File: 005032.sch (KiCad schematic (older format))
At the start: 38 parts, among them J1 alim+conn, J2 PROG_ESP02, J4 JTAG, SW1 DMR02, SW2 434153017835, SW3 434153017835, U1 ESP32-WROOM-32E, U2 AP63201, U3 AP63357

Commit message: v5 - commit prima di esecuzione modifiche v6
Signed-off-by: Andrea Toninelli <tonazza@yahoo.it>
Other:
- note added: "MODULO MCU - WIFI"
- note removed: "MODULO MCU"
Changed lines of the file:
@@
 NoConn ~ 3200 3200
 Text Notes 850  850  0    118  ~ 0
-MODULO MCU
+MODULO MCU - WIFI
 Wire Notes Line
 	7000 1750 7000 550

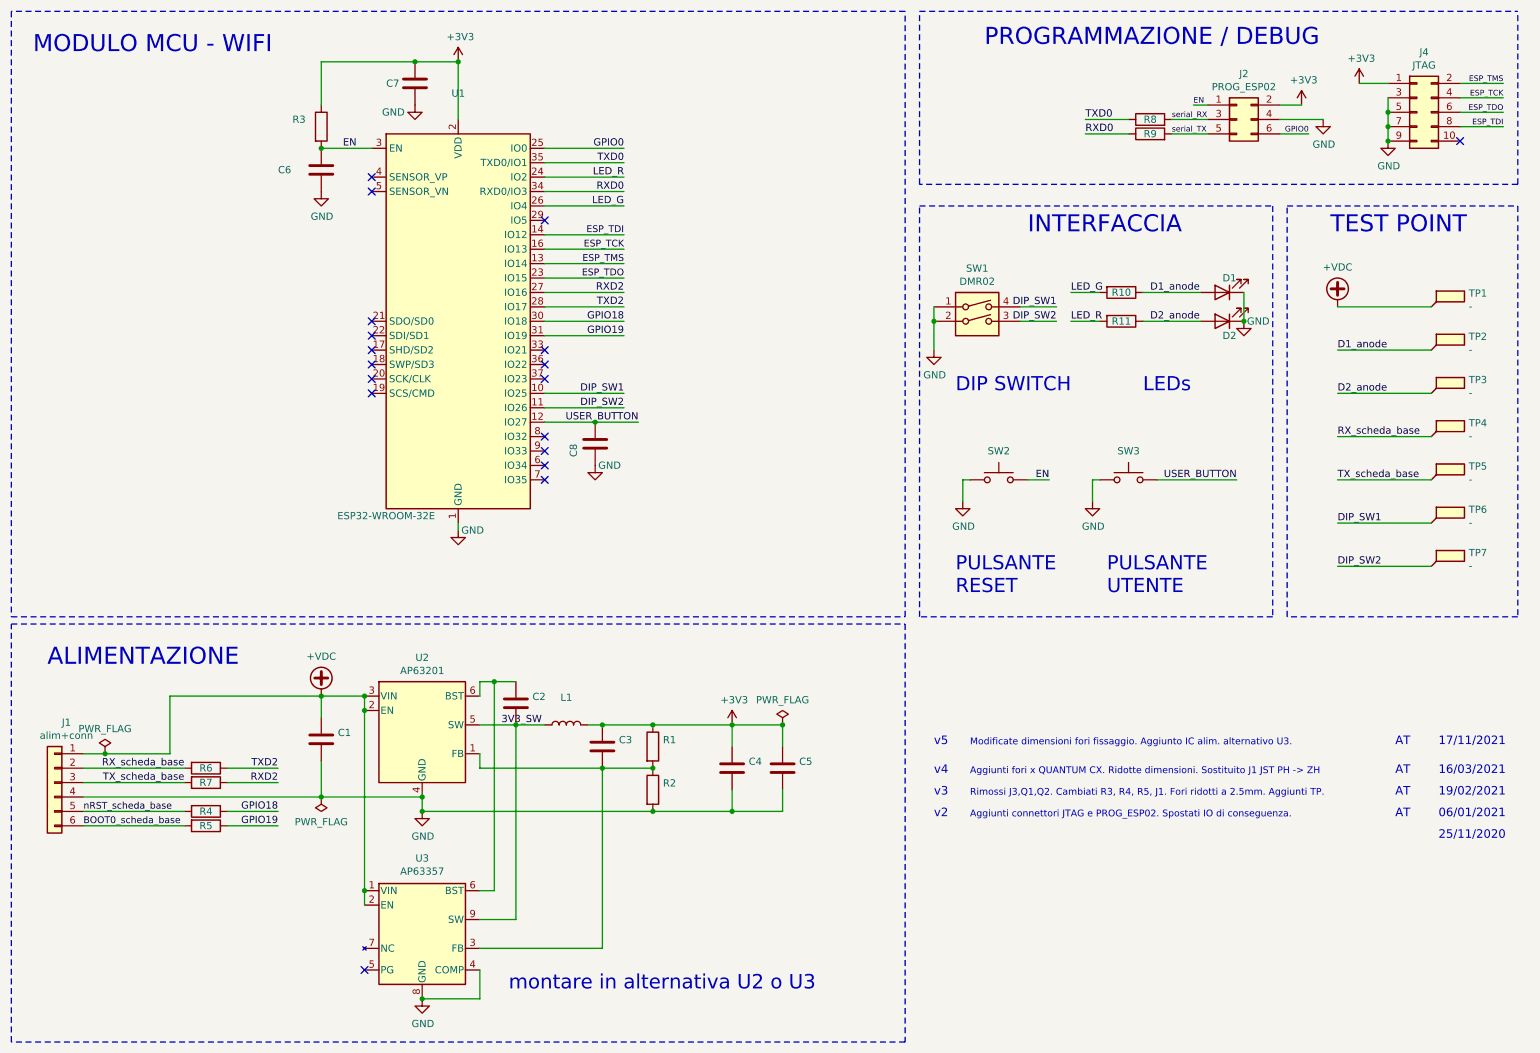
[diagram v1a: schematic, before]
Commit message: v6 - modificato schema (PCB ancora in v5)
Signed-off-by: Andrea Toninelli <tonazza@yahoo.it>
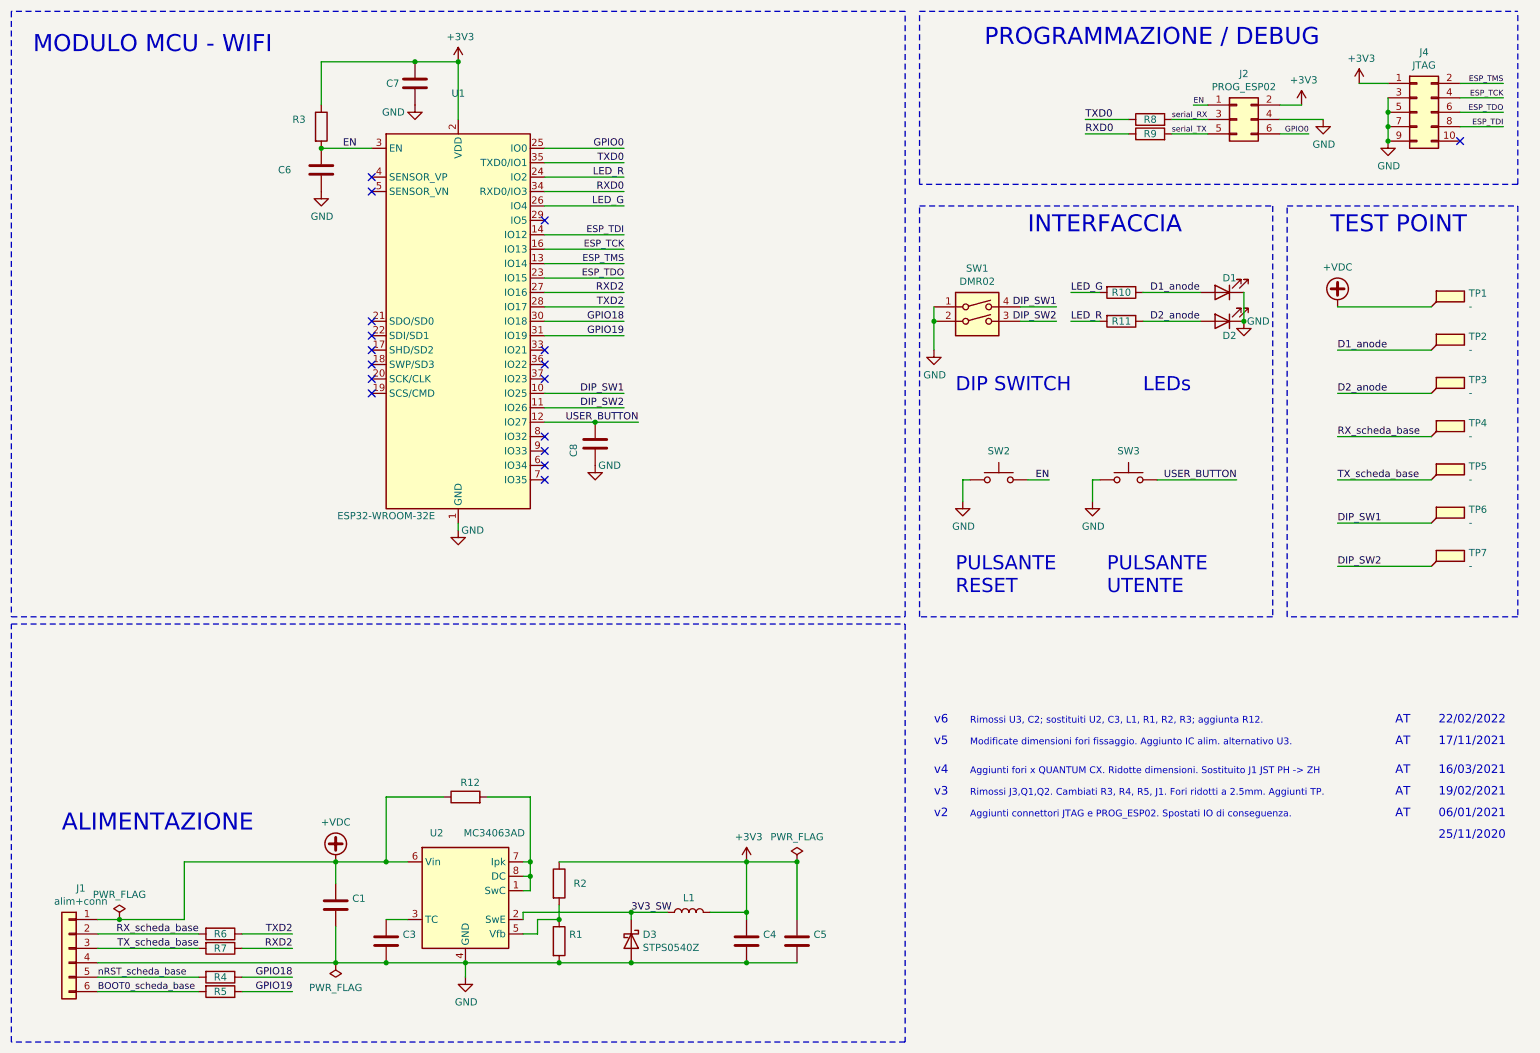
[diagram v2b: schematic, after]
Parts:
- removed C2: 0.1u, Capacitor_SMD:C_0603_1608Metric, symbol Device:C
- removed U2: AP63201, Package_TO_SOT_SMD:SOT-23-6, symbol 005032-rescue:AP63201-@tonazza
- removed U3: AP63357, aerauliqa-IC:AP6335x, symbol @tonazza:AP63357
- added D3: STPS0540Z, Diode_SMD:D_SOD-123, symbol Device:D_Schottky
- added R12: 0R33 1%, Resistor_SMD:R_1206_3216Metric_Pad1.42x1.75mm_HandSolder, symbol Device:R
- added U2: MC34063AD, Package_SO:SOIC-8_3.9x4.9mm_P1.27mm, symbol Regulator_Switching:MC34063AD
- C3: value 100p -> 220p; CMP_DB_AQ CAP00-000-039 -> CAP00-000-011
- L1: value NRS4018T6R8‎ -> NRS5030T220MMGJ; footprint Inductor_SMD:L_Taiyo-Yuden_NR-40xx -> Inductor_SMD:L_Taiyo-Yuden_NR-50xx; CMP_DB_AQ IND00-000-039 -> IND00-000-040
- R1: value 180K 1% -> 11K 1%; CMP_DB_AQ RES00-000-104 -> RES00-000-108
- R2, R3: value 57.6K 1% -> 18K 1%; CMP_DB_AQ RES00-000-103 -> RES00-000-046
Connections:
- net +3V3: now also R2.1; no longer C3.1, R1.1
- net +VDC: now also R12.1, U2.6 (Vin)
- net 3V3_SW: now also D3.1 (K), U2.2 (SwE)
- net GND: now also C3.2, R1.2, D3.2 (A), U2.4 (GND); no longer R2.2
- new net: C3.1, U2.3 (TC)
- new net: R1.1, R2.2, U2.5 (Vfb)
- new net: R12.2, U2.1 (SwC), U2.7 (Ipk), U2.8 (DC)
- no-connect marks 18 -> 17
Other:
- note added: "22/02/2022"
- note added: "Rimossi U3, C2; sostituiti U2, C3, L1, R1, R2, R3; aggiunta R12."
- note added: "v6"
- note removed: "montare in alternativa U2 o U3"
- moved on the sheet: C1, C3, C4, C5, J1, L1, R1, R4, R5, R6, R7

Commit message: v6 - modificato PCB (TEMP - in attesa revisione meccanica per montaggio su QUANTUM EX 100/150)
Signed-off-by: Andrea Toninelli <tonazza@yahoo.it>
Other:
- note added: "Rimossi U3, C2; sostituiti U2, C3, L1, R1, R2, R3; aggiunti R12, D3."
- note removed: "Rimossi U3, C2; sostituiti U2, C3, L1, R1, R2, R3; aggiunta R12."
- moved on the sheet: C1, C3, C4, C5, D3, J1, L1, R1, R12, R2, R4, R5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
